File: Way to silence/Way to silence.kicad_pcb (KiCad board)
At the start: 2 copper layers, 57.9 x 38.1 mm, 62 parts, among them J1 SD Card Connector, J2 Amplificator_Terminal, J3 5V_Terminal, J4 Battery_Terminal, Q1 BC817, Q2 BC817, SW1 SW_SPDT, U1 ESP32-WROOM-32-N16, U2 SM5308, U3 CP2102-GMR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

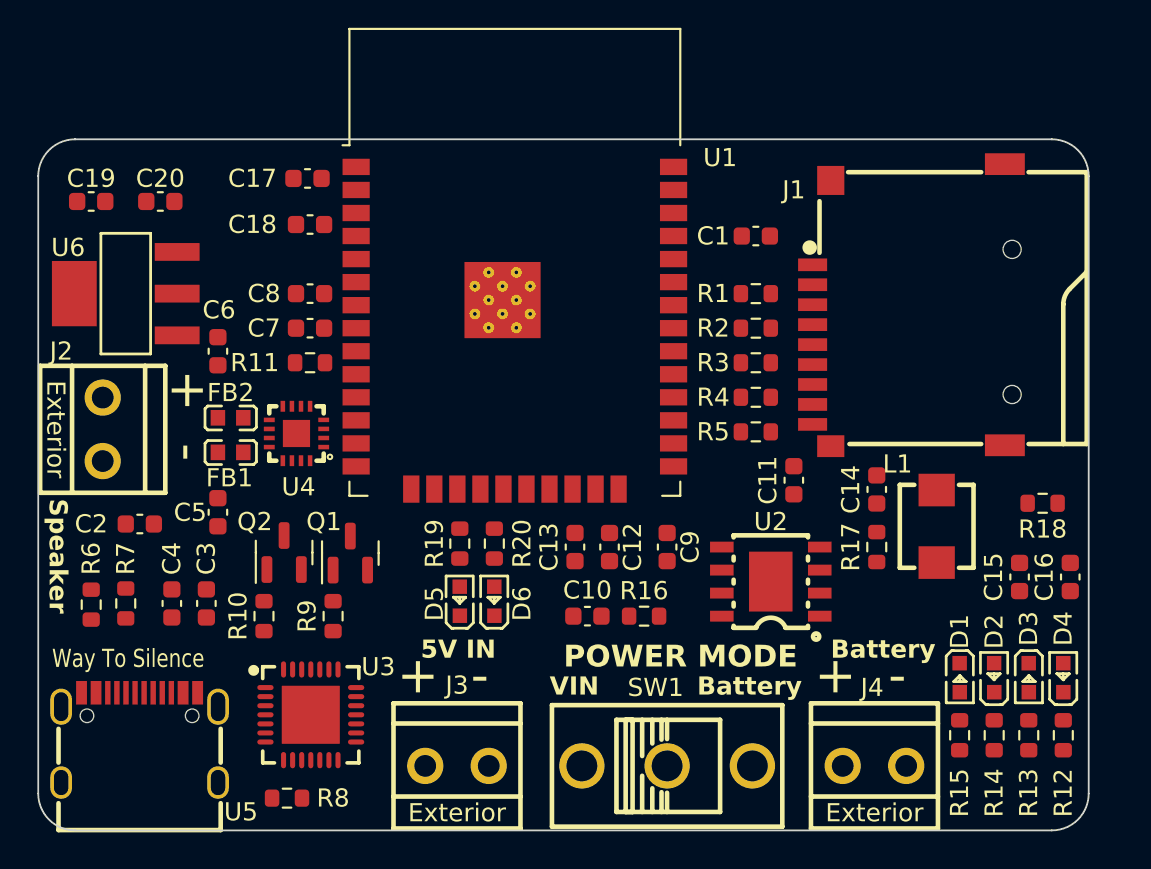
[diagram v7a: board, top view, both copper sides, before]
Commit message: [ADD] Update for mounting holes
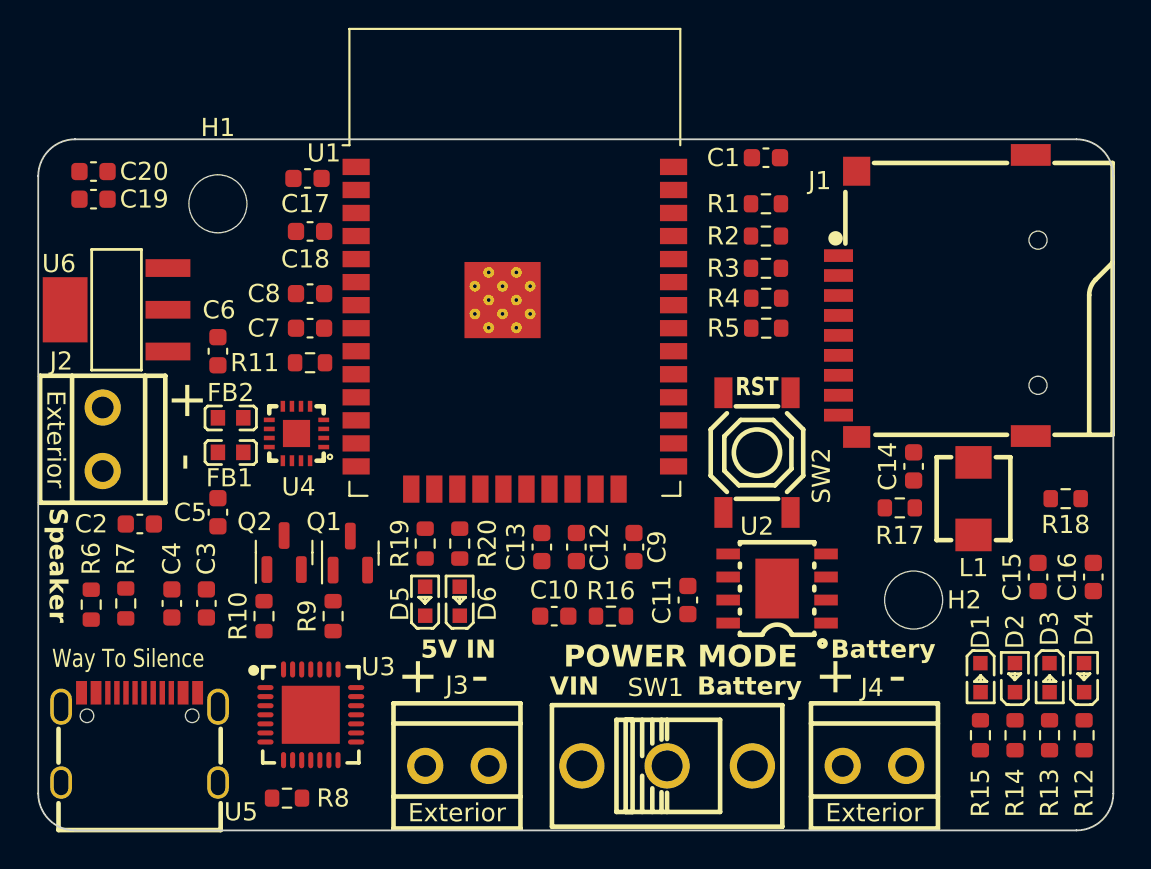
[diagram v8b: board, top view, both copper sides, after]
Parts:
- added H1: MountingHole, Way to silence:MountingHole_3.2mm_M3, F.Cu at (73.7, 47.8)
- added H2: MountingHole, Way to silence:MountingHole_3.2mm_M3, F.Cu at (112.0, 69.6)
- added SW2: SW_MEC_5E, Way to silence:TS-1187A, F.Cu at (103.4, 61.5)
- moved C11 8.82 mm to (99.6, 69.6)
- moved R5 5.74 mm to (103.9, 54.6)
- moved R4 5.49 mm to (103.9, 53.0)
- moved R3 5.24 mm to (103.9, 51.3)
- moved R2 5.11 mm to (103.9, 49.5)
- moved R1 4.98 mm to (103.9, 47.8)
- moved C1 4.35 mm to (103.9, 45.2)
- moved C20 4.04 mm to (66.8, 46.0), turned to 0 degrees
- moved L1 2.54 mm to (115.3, 64.0)
- moved R17 2.50 mm to (111.3, 64.5), turned to 0 degrees
- moved C14 2.40 mm to (112.0, 62.2)
- moved D5 1.91 mm to (85.1, 69.7)
- moved D6 1.91 mm to (87.0, 69.7)
- moved R19 1.91 mm to (85.1, 66.5)
- moved R20 1.91 mm to (87.0, 66.5)
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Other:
- board size 57.9 x 38.1 mm -> 59.3 x 38.1 mm
- board text added: "RST"
